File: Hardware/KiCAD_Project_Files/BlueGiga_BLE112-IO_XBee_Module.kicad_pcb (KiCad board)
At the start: 4 copper layers, 31 x 24.4 mm, 10 parts, among them P1 XBEE HEADER, P2 DEBUG, P3 HEADER_M_2.54MM_2R20P_ST_AU_P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, U1 BLE112-A

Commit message: Rev 1.0 complete.  Updated all KiCAD project files and generated gerbers.
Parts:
- C1, C2, C3, C4, C5, C6: footprint C0603 -> Passive:C0603
- P1: footprint HEADER_XBEE -> Header:HEADER_XBEE
- P2: footprint HEADER_50MIL_2R10P_SMT -> Header:HEADER_50MIL_2R10P_SMT
- U1: footprint BLE112 -> RF_Modules:BLE112
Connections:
- P1 pad 11: Net-(P1-Pad11) -> (no net)
- P1 pad 13: Net-(P1-Pad13) -> (no net)
- P1 pad 14: Net-(P1-Pad14) -> (no net)
- P1 pad 15: Net-(P1-Pad15) -> (no net)
- P1 pad 17: Net-(P1-Pad17) -> (no net)
- P1 pad 18: Net-(P1-Pad18) -> (no net)
- P1 pad 19: Net-(P1-Pad19) -> (no net)
- P1 pad 20: Net-(P1-Pad20) -> (no net)
- P1 pad 4: Net-(P1-Pad4) -> (no net)
- P1 pad 6: Net-(P1-Pad6) -> (no net)
- P1 pad 7: Net-(P1-Pad7) -> (no net)
- P1 pad 8: Net-(P1-Pad8) -> (no net)
- P1 pad 9: Net-(P1-Pad9) -> (no net)
- P2 pad 10: Net-(P2-Pad10) -> (no net)
- P2 pad 5: Net-(P2-Pad5) -> (no net)
- P2 pad 6: Net-(P2-Pad6) -> (no net)
- P2 pad 8: Net-(P2-Pad8) -> (no net)
- P2 pad 9: +3V3 -> (no net)
- U1 pad 11: USB+ -> (no net)
- U1 pad 12: USB- -> (no net)
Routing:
- net +3V3: track 30.9 -> 29.3 mm, vias 7 -> 6

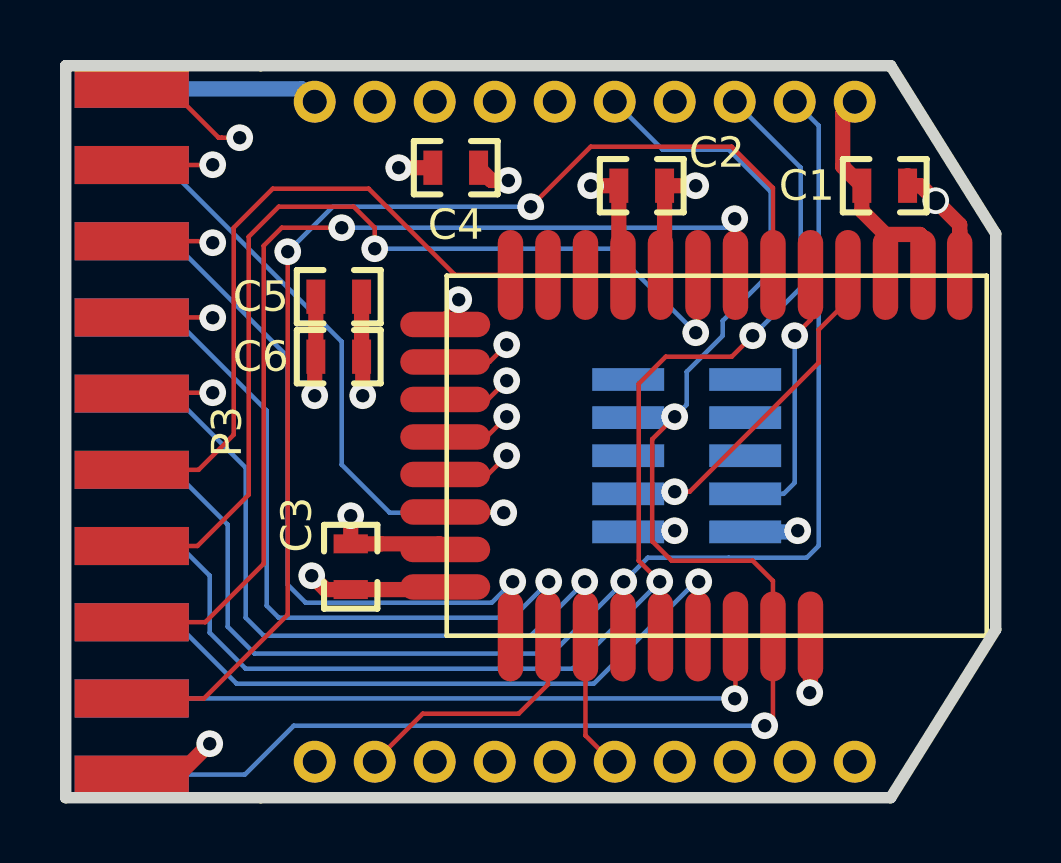
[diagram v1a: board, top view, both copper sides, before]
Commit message: Changed schematic and board layout to conform to BlueGiga's usage of USART1 ALT1.
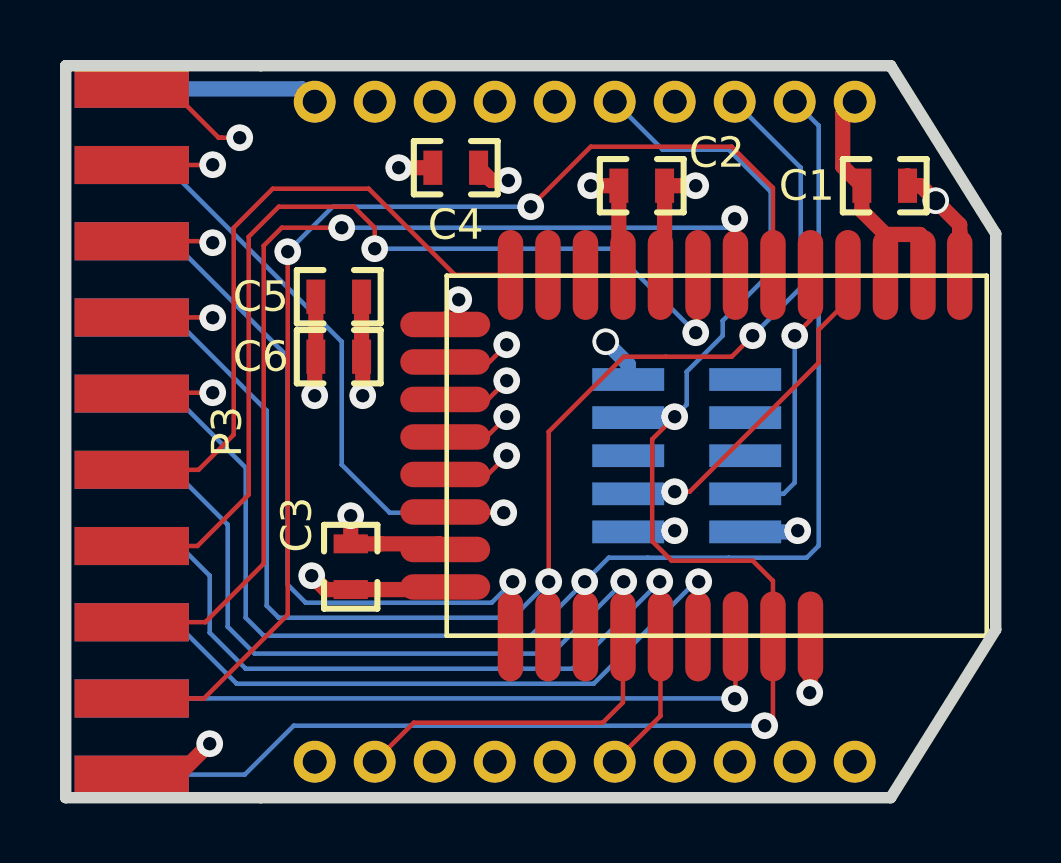
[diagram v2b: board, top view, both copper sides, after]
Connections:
- P2 pad 9: (no net) -> +3V3
- P3 pad 10: P0_3/TX -> P0_5/RT
- P3 pad 12: P0_4/CT -> P0_3/TX
- P3 pad 14: P0_5/RT -> P0_2/RX
- P3 pad 8: P0_2/RX -> P0_4/CT
- U1 pad 23: P0_5/RT -> P0_2/RX
- U1 pad 24: P0_4/CT -> P0_3/TX
- U1 pad 25: P0_3/TX -> P0_5/RT
- U1 pad 26: P0_2/RX -> P0_4/CT
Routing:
- net P0_2/RX: track 44.2 -> 46.7 mm
- net P0_5/RT: track 32.6 -> 35.0 mm
- net +3V3: track 29.3 -> 30.8 mm, vias 6 -> 7
- net P0_3/TX: track 45.9 -> 47.4 mm
